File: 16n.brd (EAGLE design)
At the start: 248.9 x 120.7 mm, 110 parts, among them J1 PJ302M, J10 PJ302M, J11 PJ302M, J12 PJ302M, J13 PJ302M, J14 PJ302M, J15 PJ302M, J16 PJ302M, J2 PJ302M, J3 PJ302M, J4 PJ302M, J5 PJ302M, J6 PJ302M, J7 PJ302M, J8 PJ302M, J9 PJ302M, U1 MCP6004_SMD, U2 MCP6004_SMD, U3 MCP6004_SMD, U4 MCP6004_SMD, U5 MCP6004_SMD, U6 MCP6004_SMD, U7 MCP6004_SMD, U8 MCP6004_SMD

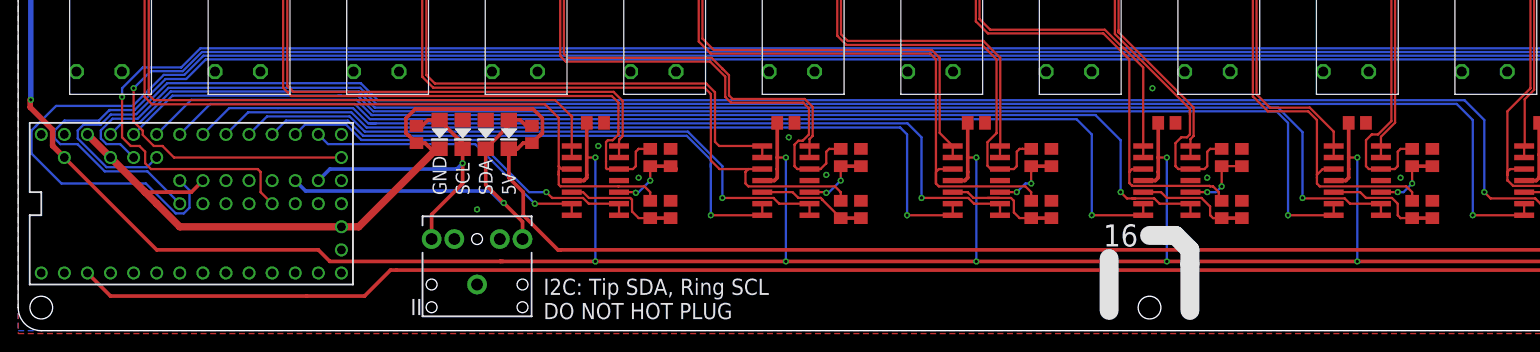
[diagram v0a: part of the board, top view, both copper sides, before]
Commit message: Moved teensy 25mil north.
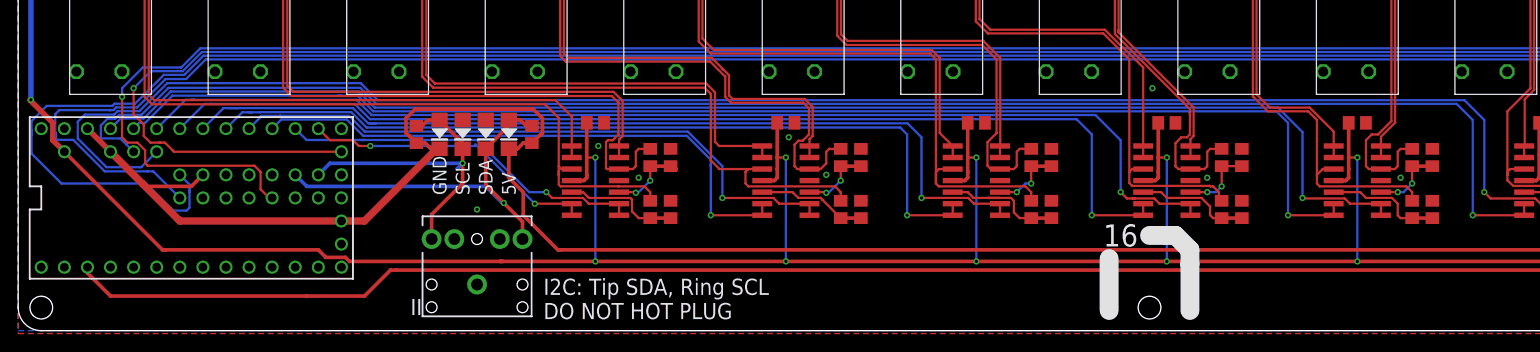
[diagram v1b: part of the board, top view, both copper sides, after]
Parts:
- moved U$1 0.63 mm to (20.3, 14.6)
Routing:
- net A12: track 221.1 -> 223.0 mm
- net A13: track 236.3 -> 237.7 mm
- net A3: track 69.8 -> 71.0 mm
- net A11: track 189.2 -> 190.0 mm
- net A5: track 99.1 -> 99.7 mm
- net SCL: track 35.0 -> 35.7 mm
- net MIDI_OUT: track 222.9 -> 223.6 mm
- net A0: track 32.3 -> 32.9 mm, vias 1 -> 2

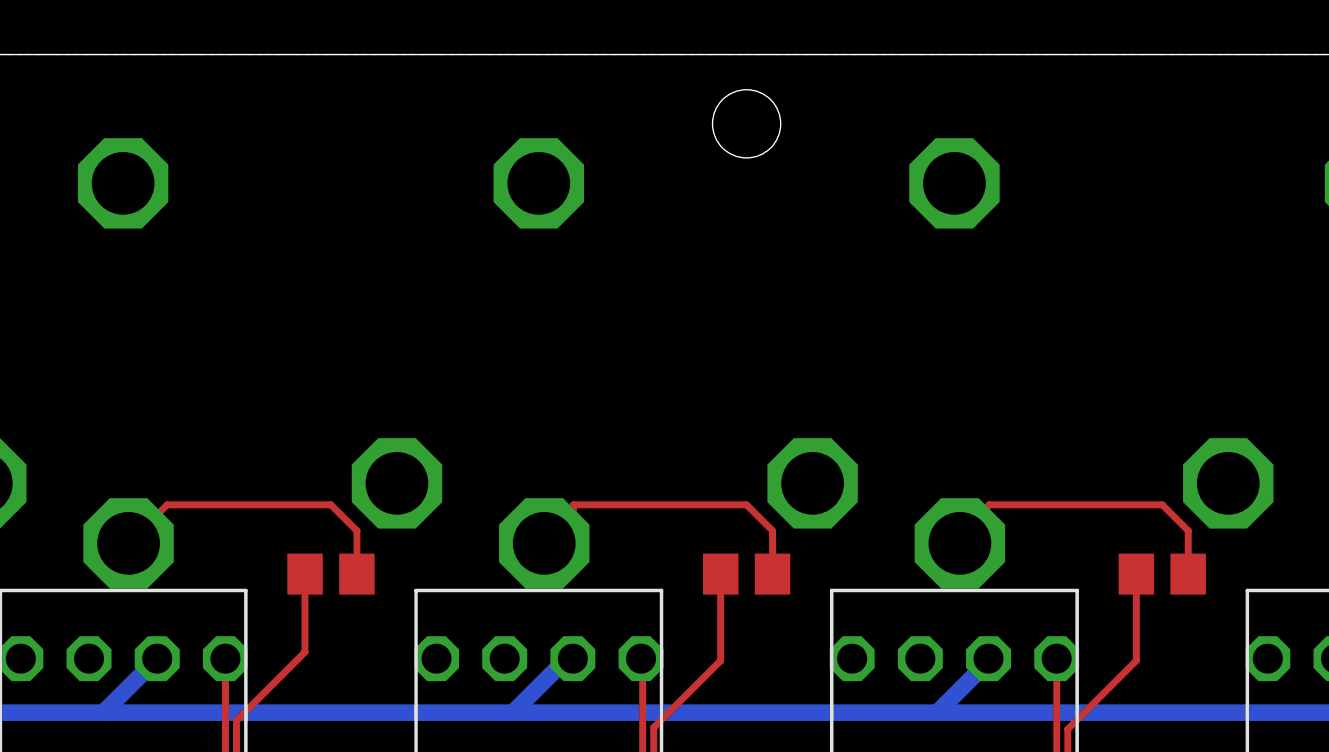
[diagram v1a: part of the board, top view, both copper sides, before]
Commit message: Space around M2.5 holes.
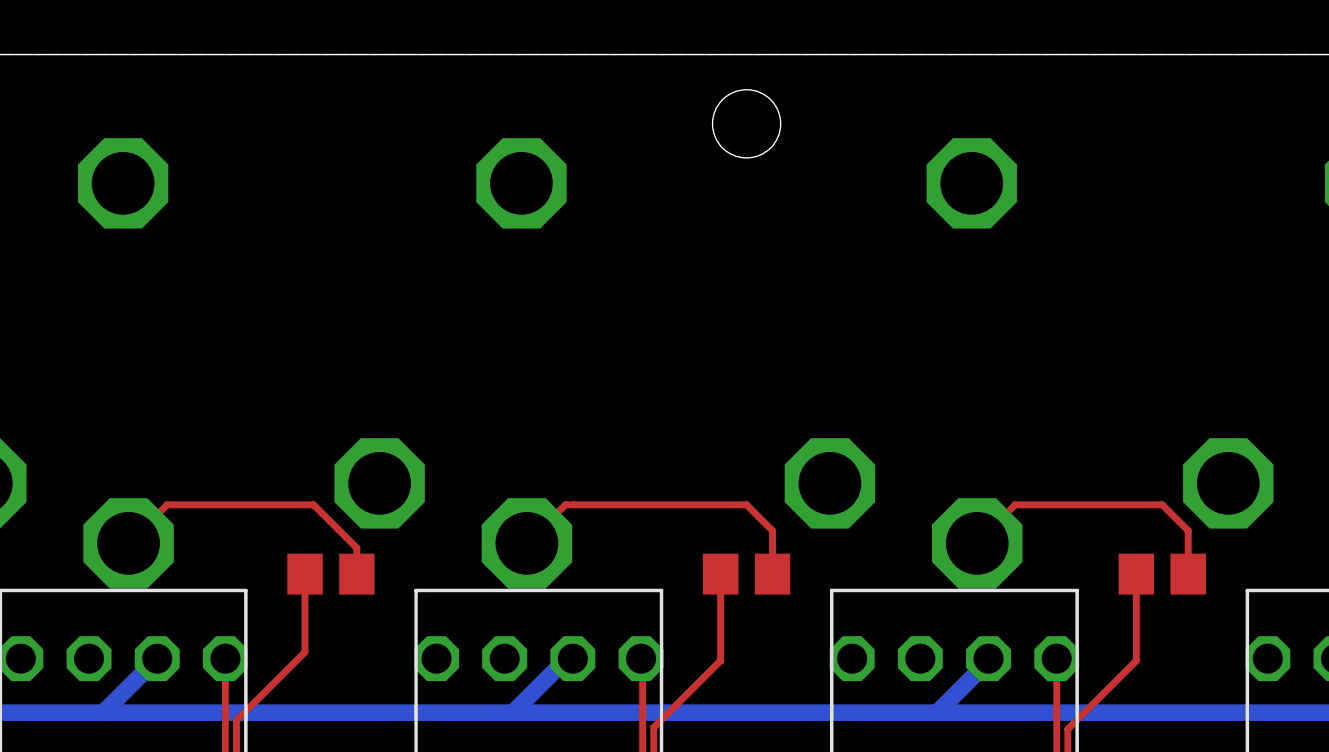
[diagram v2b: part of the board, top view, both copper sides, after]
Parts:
- moved J8 0.64 mm to (116.2, 118.4)
- moved J9 0.63 mm to (132.7, 118.4)
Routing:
- net CV9: track 11.1 -> 10.3 mm
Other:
- board text added: "v1.25"
- board text removed: "v1.21"
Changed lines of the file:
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@@
 </layers>
 <board>
+<fusionsync huburn="a.cGVyc29uYWw6dWUyOTViNDRl" projecturn="a.cGVyc29uYWw6dWUyOTViNDRlIzIwMTgwMTA4MTExMjk1Mzc2" f3durn="urn:adsk.wipprod:dm.lineage:1LPsho2iRQCPn5uxACv-6A" pcbguid="234bef35-d82d-46ce-857c-37a291aa7fed" lastpulledtime="" lastsyncedchangeguid="997eabcc-99a1-b09b-9ab4-6687188ddba9"/>
 <plain>
 <wire x1="2.54" y1="0" x2="246.38" y2="0" width="0" layer="20"/>
@@
 Tom Armitage
 Brendan Cassidy</text>
-<text x="240.665" y="63.5" size="1.0668" layer="26" ratio="10" rot="MR0" align="top-left">v1.21</text>
+<text x="240.665" y="63.5" size="1.0668" layer="26" ratio="10" rot="MR0" align="top-left">v1.25</text>
 <text x="57.785" y="1.27" size="1.778" layer="25">I2C: Tip SDA, Ring SCL
 DO NOT HOT PLUG</text>
@@
 <element name="J6" library="pj302m" package="PJ302M" value="PJ302M" x="86.36" y="118.4275" smashed="yes" rot="R270"/>
 <element name="J7" library="pj302m" package="PJ302M" value="PJ302M" x="101.6" y="118.4275" smashed="yes" rot="R270"/>
-<element name="J8" library="pj302m" package="PJ302M" value="PJ302M" x="116.84" y="118.4275" smashed="yes" rot="R270"/>
-<element name="J9" library="pj302m" package="PJ302M" value="PJ302M" x="132.08" y="118.4275" smashed="yes" rot="R270"/>
+<element name="J8" library="pj302m" package="PJ302M" value="PJ302M" x="116.205" y="118.4275" smashed="yes" rot="R270"/>
+<element name="J9" library="pj302m" package="PJ302M" value="PJ302M" x="132.715" y="118.4275" smashed="yes" rot="R270"/>
 <element name="J10" library="pj302m" package="PJ302M" value="PJ302M" x="147.32" y="118.4275" smashed="yes" rot="R270"/>
 <element name="J11" library="pj302m" package="PJ302M" value="PJ302M" x="162.56" y="118.4275" smashed="yes" rot="R270"/>
@@
 <contactref element="J7" pad="TIP"/>
 <wire x1="101.8" y1="102.7275" x2="103.2125" y2="104.14" width="0.254" layer="1"/>
-<wire x1="109.22" y1="104.14" x2="103.2125" y2="104.14" width="0.254" layer="1"/>
-<wire x1="110.1725" y1="103.1875" x2="109.22" y2="104.14" width="0.254" layer="1"/>
+<wire x1="108.585" y1="104.14" x2="103.2125" y2="104.14" width="0.254" layer="1"/>
 <contactref element="R22" pad="2"/>
-<wire x1="110.17" y1="101.6" x2="110.1725" y2="101.6025" width="0.254" layer="1"/>
-<wire x1="110.1725" y1="101.6025" x2="110.1725" y2="103.1875" width="0.254" layer="1"/>
+<wire x1="110.17" y1="101.6" x2="110.17" y2="102.555" width="0.254" layer="1"/>
+<wire x1="110.17" y1="102.555" x2="108.585" y2="104.14" width="0.254" layer="1"/>
 </signal>
 <signal name="CV8">
 <contactref element="J8" pad="TIP"/>
 <contactref element="R46" pad="2"/>
-<wire x1="117.04" y1="102.7275" x2="118.11" y2="103.7975" width="0.254" layer="1"/>
-<wire x1="118.11" y1="103.7975" x2="118.11" y2="104.14" width="0.254" layer="1"/>
 <wire x1="118.11" y1="104.14" x2="124.46" y2="104.14" width="0.254" layer="1"/>
 <wire x1="124.46" y1="104.14" x2="125.41" y2="103.19" width="0.254" layer="1"/>
 <wire x1="125.41" y1="103.19" x2="125.41" y2="101.6" width="0.254" layer="1"/>
+<wire x1="116.405" y1="102.7275" x2="117.8175" y2="104.14" width="0.254" layer="1"/>
+<wire x1="117.8175" y1="104.14" x2="118.11" y2="104.14" width="0.254" layer="1"/>
 </signal>
 <signal name="CV10">
@@
 <contactref element="J9" pad="TIP"/>
 <contactref element="R27" pad="2"/>
-<wire x1="132.28" y1="102.7275" x2="132.28" y2="103.07" width="0.254" layer="1"/>
-<wire x1="132.28" y1="103.07" x2="133.35" y2="104.14" width="0.254" layer="1"/>
-<wire x1="133.35" y1="104.14" x2="139.7" y2="104.14" width="0.254" layer="1"/>
+<wire x1="134.3025" y1="104.14" x2="139.7" y2="104.14" width="0.254" layer="1"/>
 <wire x1="139.7" y1="104.14" x2="140.6525" y2="103.1875" width="0.254" layer="1"/>
 <wire x1="140.6525" y1="103.1875" x2="140.6525" y2="101.6025" width="0.254" layer="1"/>
 <wire x1="140.6525" y1="101.6025" x2="140.65" y2="101.6" width="0.254" layer="1"/>
+<wire x1="132.915" y1="102.7275" x2="132.915" y2="102.7525" width="0.254" layer="1"/>
+<wire x1="132.915" y1="102.7525" x2="134.3025" y2="104.14" width="0.254" layer="1"/>
 </signal>
 <signal name="N$9">
@@
 </note>
 <note version="8.3" severity="warning">
+Since Version 8.3, EAGLE supports Fusion synchronisation.
+This feature will not be available in this version and saving
+the document will break the link to the Fusion PCB feature.
+</note>
+<note version="8.3" severity="warning">

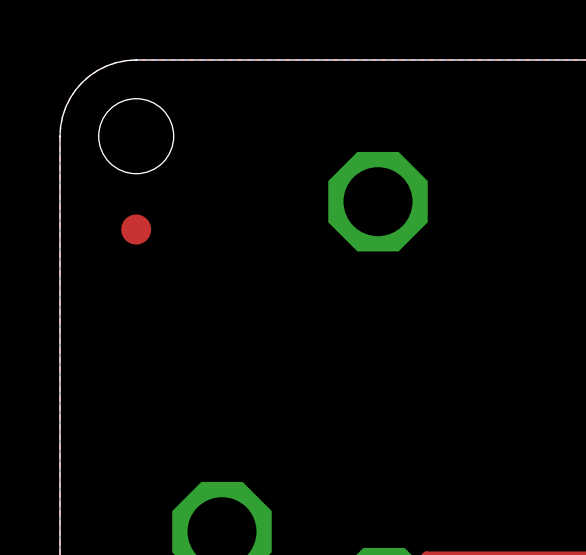
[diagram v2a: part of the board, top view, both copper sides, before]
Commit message: Eagle 9.1.0 version BRD: added CC licence/logo.
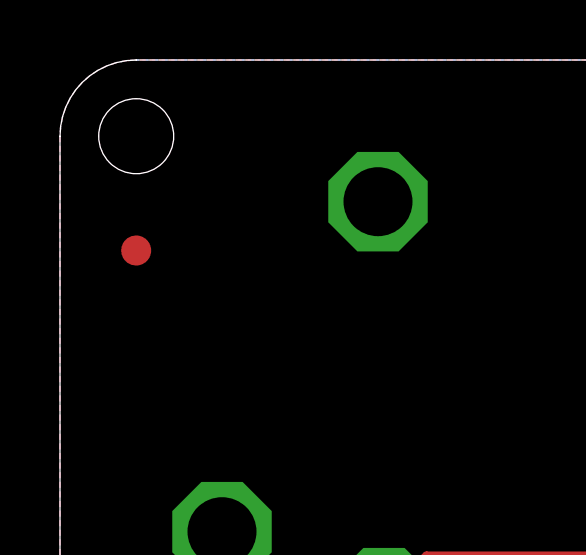
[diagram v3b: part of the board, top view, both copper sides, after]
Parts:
- moved FID1 0.70 mm to (2.54, 114.3)
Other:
- board text added: "CC-BY-SA 4.0"
- board text added: "Creative Commons Attribution / ShareAlike"

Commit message: 1.26 - tidying and CC logo.
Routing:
- net A5: track 99.7 -> 98.2 mm
- net A3: track 71.0 -> 69.7 mm
- net N$12: track 14.1 -> 12.8 mm
- net A12: track 223.0 -> 221.7 mm
- net N$2: track 20.6 -> 19.5 mm
- net SCL: track 35.7 -> 34.8 mm
- net A7: track 125.2 -> 124.4 mm
- net A13: track 237.7 -> 237.1 mm
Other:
- board text added: "v1.26"
- board text removed: "v1.25"
